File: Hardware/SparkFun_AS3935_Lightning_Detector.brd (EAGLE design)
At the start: 25.4 x 25.4 mm, 57 parts, among them U1 AS3935

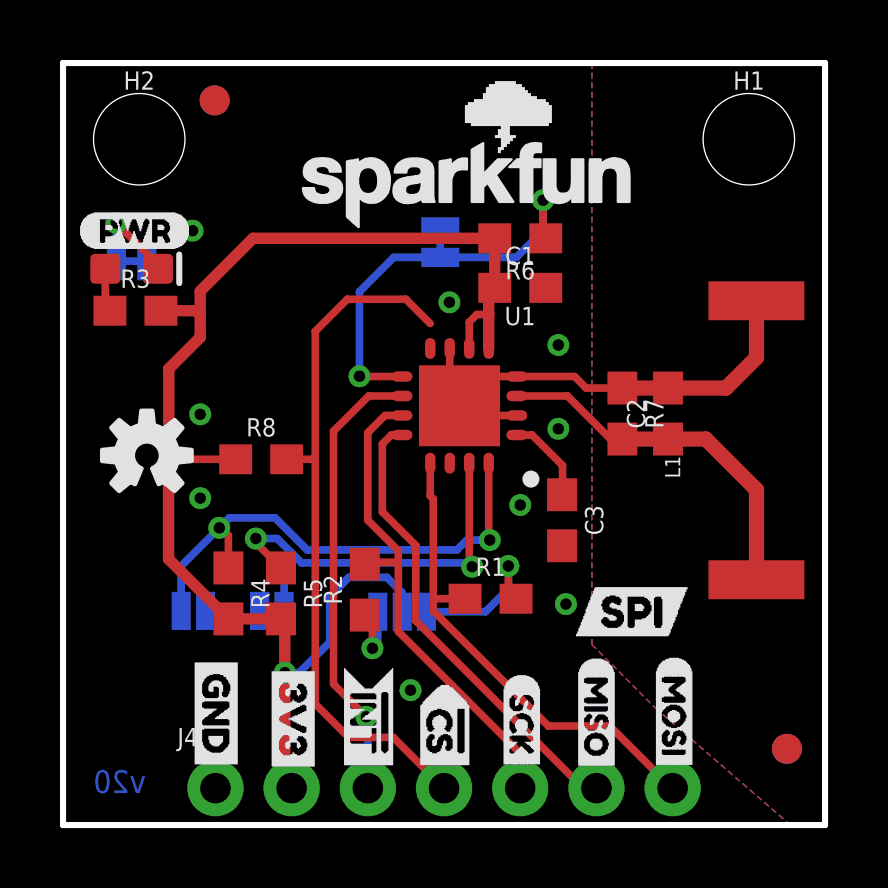
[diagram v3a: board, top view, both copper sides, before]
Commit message: Adds three way jumper for switching to I2C, one that also includes a way to ground Chip select
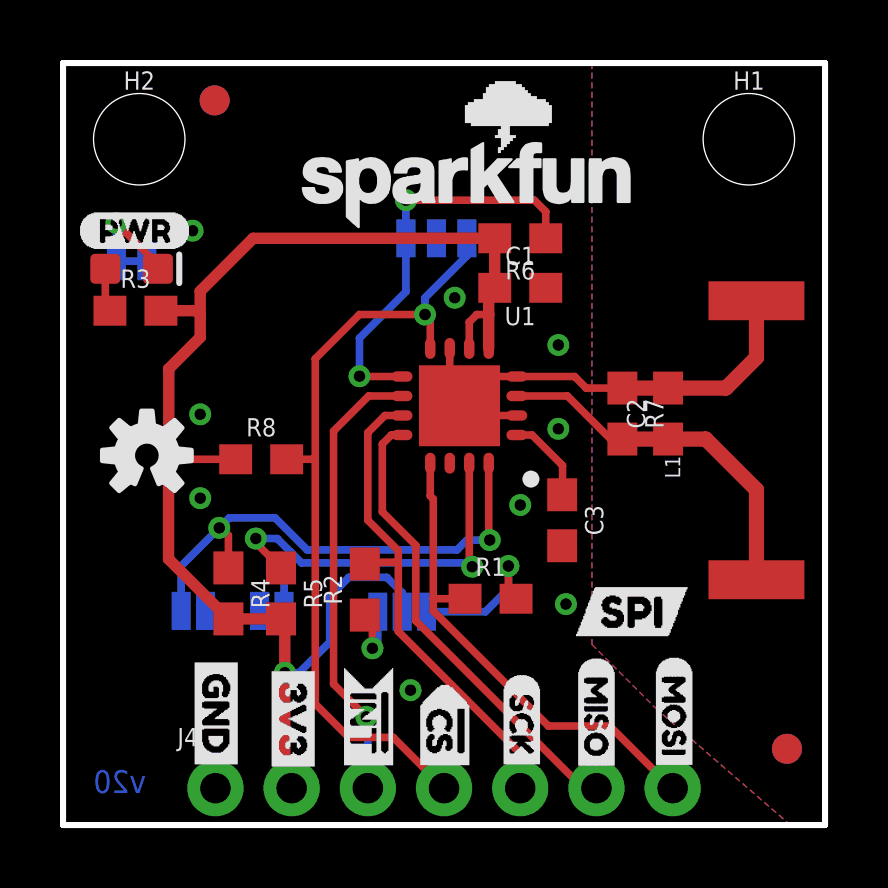
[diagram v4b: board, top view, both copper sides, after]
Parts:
- removed JP3: JUMPER-SMT_2_NC_TRACE_SILK, SparkFun-Jumpers:SMT-JUMPER_2_NC_TRACE_SILK
- added JP1: I2C_EN, SparkFun-Jumpers:SMT-JUMPER_3_1-NC_TRACE_SILK
- added U$16: (no value), CS and SI:CS0
- added U$19: (no value), CS and SI:SI1
- moved U$17 0.15 mm to (15.4, 21.7)
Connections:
- net !CS: now also JP1.1
- net GND: now also JP1.2; no longer JP3.2
- net SEL_INTER: now also JP1.3; no longer JP3.1
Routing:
- net !CS: track 23.4 -> 26.5 mm, vias 0 -> 1
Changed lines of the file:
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@@
 <attribute name="VALUE" value="10k" x="15.24" y="20.32" size="0.6096" layer="27" font="vector" ratio="20" rot="R180" align="top-center"/>
-</element>
-<element name="JP3" library="SparkFun-Jumpers" package="SMT-JUMPER_2_NC_TRACE_SILK" value="JUMPER-SMT_2_NC_TRACE_SILK" x="12.573" y="19.431" smashed="yes" rot="MR90">
-<attribute name="NAME" x="13.716" y="19.431" size="0.6096" layer="26" font="vector" ratio="20" rot="MR90" align="bottom-center"/>
-<attribute name="VALUE" x="11.43" y="19.431" size="0.6096" layer="28" font="vector" ratio="20" rot="MR90" align="top-center"/>
 </element>
 <element name="J4" library="SparkFun-Connectors" package="1X07_NO_SILK" value="" x="5.08" y="1.229359375" smashed="yes">
@@
 <element name="U$14" library="INT" package="#INT0" value="" x="10.1854" y="5.5118" smashed="yes" rot="MR270"/>
 <element name="U$15" library="DataLines" package="SPI1" value="" x="21.082" y="7.112" smashed="yes" rot="MR0"/>
-<element name="U$17" library="i2c_EN" package="I#C_EN0" value="" x="15.5194" y="21.6916" smashed="yes" rot="MR0"/>
+<element name="U$17" library="i2c_EN" package="I#C_EN0" value="" x="15.367" y="21.6916" smashed="yes" rot="MR0"/>
+<element name="JP1" library="SparkFun-Jumpers" package="SMT-JUMPER_3_1-NC_TRACE_SILK" value="I2C_EN" x="12.446" y="19.558" smashed="yes" rot="MR0">
+<attribute name="NAME" x="12.446" y="20.701" size="0.6096" layer="26" font="vector" ratio="20" rot="MR0" align="bottom-center"/>
+<attribute name="VALUE" x="12.446" y="18.415" size="0.6096" layer="28" font="vector" ratio="20" rot="MR0" align="top-center"/>
+</element>
+<element name="U$16" library="CS and SI" package="CS0" value="" x="15.0622" y="21.3868" smashed="yes" rot="MR270"/>
+<element name="U$19" library="CS and SI" package="SI1" value="" x="9.779" y="21.0312" smashed="yes" rot="MR270"/>
 </elements>
 <signals>
@@
 <contactref element="ADD0" pad="2"/>
 <contactref element="ADD1" pad="2"/>
-<contactref element="JP3" pad="2"/>
 <contactref element="J4" pad="1"/>
 <contactref element="C3" pad="2"/>
@@
 <via x="16.51" y="13.208" extent="1-16" drill="0.381"/>
 <via x="16.51" y="16.002" extent="1-16" drill="0.381"/>
-<via x="12.8778" y="17.4244" extent="1-16" drill="0.381"/>
+<via x="13.0556" y="17.5768" extent="1-16" drill="0.381"/>
 <via x="4.318" y="19.812" extent="1-16" drill="0.381"/>
 <wire x1="12.8896" y1="15.8866" x2="12.8896" y2="14.3016" width="0.254" layer="1"/>
@@
 <wire x1="23.114" y1="15.582" x2="23.114" y2="17.477" width="0.508" layer="1"/>
 <via x="4.572" y="10.8966" extent="1-16" drill="0.381"/>
+<contactref element="JP1" pad="2"/>
 </signal>
 <signal name="3.3V">
@@
 <signal name="SEL_INTER">
 <contactref element="R6" pad="1"/>
-<contactref element="JP3" pad="1"/>
 <contactref element="U1" pad="9"/>
-<via x="16.002" y="20.828" extent="1-16" drill="0.381"/>
-<wire x1="15.113" y1="18.923" x2="16.002" y2="19.812" width="0.254" layer="16"/>
-<wire x1="16.002" y1="19.812" x2="16.002" y2="20.828" width="0.254" layer="16"/>
-<wire x1="16.09" y1="19.558" x2="16.002" y2="19.646" width="0.254" layer="1"/>
-<wire x1="16.002" y1="19.646" x2="16.002" y2="20.828" width="0.254" layer="1"/>
 <wire x1="11.2996" y1="14.9516" x2="9.8896" y2="14.9516" width="0.254" layer="1"/>
 <wire x1="9.8806" y1="14.9606" x2="9.8896" y2="14.9516" width="0.254" layer="1"/>
 <via x="9.8806" y="14.9606" extent="1-16" drill="0.381"/>
-<wire x1="9.8806" y1="14.9606" x2="9.8806" y2="17.78" width="0.254" layer="16"/>
-<wire x1="9.8806" y1="17.78" x2="11.0236" y2="18.923" width="0.254" layer="16"/>
-<wire x1="11.0236" y1="18.923" x2="12.573" y2="18.923" width="0.254" layer="16"/>
-<wire x1="12.573" y1="18.923" x2="15.113" y2="18.923" width="0.254" layer="16"/>
+<contactref element="JP1" pad="3"/>
+<wire x1="11.43" y1="19.558" x2="11.43" y2="19.3294" width="0.2032" layer="16"/>
+<wire x1="11.43" y1="17.78" x2="11.43" y2="19.558" width="0.254" layer="16"/>
+<wire x1="9.8806" y1="14.9606" x2="9.8806" y2="16.2306" width="0.254" layer="16"/>
+<wire x1="9.8806" y1="16.2306" x2="11.43" y2="17.78" width="0.254" layer="16"/>
+<wire x1="11.43" y1="20.828" x2="11.43" y2="19.558" width="0.254" layer="16"/>
+<wire x1="16.09" y1="19.558" x2="16.002" y2="19.646" width="0.254" layer="1"/>
+<via x="11.43" y="20.828" extent="1-16" drill="0.381"/>
+<wire x1="16.09" y1="19.558" x2="16.09" y2="20.447" width="0.254" layer="1"/>
+<wire x1="16.09" y1="20.447" x2="15.709" y2="20.828" width="0.254" layer="1"/>
+<wire x1="15.709" y1="20.828" x2="11.43" y2="20.828" width="0.254" layer="1"/>
 </signal>
 <signal name="MISO">
@@
 <wire x1="11.008359375" y1="2.921" x2="9.525" y2="2.921" width="0.254" layer="1"/>
 <wire x1="9.525" y1="2.921" x2="8.4074" y2="4.0386" width="0.254" layer="1"/>
-<wire x1="12.2396" y1="16.7164" x2="11.43" y2="17.526" width="0.254" layer="1"/>
-<wire x1="9.4742" y1="17.526" x2="11.43" y2="17.526" width="0.254" layer="1"/>
-<wire x1="8.4074" y1="16.4592" x2="9.4742" y2="17.526" width="0.254" layer="1"/>
 <wire x1="8.4074" y1="4.0386" x2="8.4074" y2="12.192" width="0.254" layer="1"/>
-<wire x1="8.4074" y1="12.192" x2="8.4074" y2="16.4592" width="0.254" layer="1"/>
 <contactref element="U1" pad="8"/>
 <contactref element="R8" pad="2"/>
 <wire x1="7.454" y1="12.192" x2="8.4074" y2="12.192" width="0.254" layer="1"/>
-<wire x1="12.2396" y1="16.7164" x2="12.2396" y2="15.8866" width="0" layer="19" extent="1-1"/>
+<contactref element="JP1" pad="1"/>
+<wire x1="12.2396" y1="15.8866" x2="12.2428" y2="15.8898" width="0.2032" layer="1"/>
+<via x="12.065" y="17.018" extent="1-16" drill="0.381"/>
+<wire x1="13.462" y1="19.558" x2="13.462" y2="18.9738" width="0.254" layer="16"/>
+<wire x1="13.462" y1="18.9738" x2="12.065" y2="17.5768" width="0.254" layer="16"/>
+<wire x1="12.065" y1="17.5768" x2="12.065" y2="17.018" width="0.254" layer="16"/>
+<wire x1="12.065" y1="17.018" x2="9.8806" y2="17.018" width="0.254" layer="1"/>
+<wire x1="12.2396" y1="15.8866" x2="12.2396" y2="16.8434" width="0.254" layer="1"/>
+<wire x1="12.2396" y1="16.8434" x2="12.065" y2="17.018" width="0.254" layer="1"/>
+<wire x1="8.4074" y1="12.192" x2="8.4074" y2="15.5448" width="0.254" layer="1"/>
+<wire x1="8.4074" y1="15.5448" x2="9.8806" y2="17.018" width="0.254" layer="1"/>
 </signal>
 <signal name="N$2">

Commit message: Adds measurements for the standoff holes, rotates CS and SI silk, removes some wire stubs.
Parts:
- moved U$16 2.86 mm to (17.2, 19.5), turned to 0 degrees
- moved U$19 2.09 mm to (11.2, 19.5), turned to 0 degrees
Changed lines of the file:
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@@
 <layer number="45" name="Holes" color="7" fill="1" visible="yes" active="yes"/>
 <layer number="46" name="Milling" color="3" fill="1" visible="no" active="yes"/>
-<layer number="47" name="Measures" color="7" fill="1" visible="no" active="yes"/>
+<layer number="47" name="Measures" color="7" fill="1" visible="yes" active="yes"/>
 <layer number="48" name="Document" color="7" fill="1" visible="no" active="yes"/>
 <layer number="49" name="Reference" color="13" fill="1" visible="yes" active="yes"/>
@@
 <wire x1="0" y1="0" x2="25.4" y2="0" width="0.2032" layer="20"/>
 <wire x1="25.4" y1="0" x2="25.4" y2="25.4" width="0.2032" layer="20"/>
-<wire x1="25.4" y1="25.4" x2="0" y2="25.4" width="0.2032" layer="20"/>
 <wire x1="0" y1="25.4" x2="0" y2="0" width="0.2032" layer="20"/>
 <text x="19.177" y="-19.177" size="1.778" layer="51" font="vector">Elias Santistevan</text>
 <text x="2.7686" y="1.0668" size="0.762" layer="16" font="vector" ratio="15" rot="MR0">v20</text>
-<dimension x1="25.4" y1="25.4" x2="0" y2="25.4" x3="12.7" y3="28.194" textsize="1.778" textratio="15" layer="47" dtype="horizontal" unit="inch"/>
 <dimension x1="25.4" y1="0" x2="25.4" y2="25.4" x3="30.226" y3="12.7" textsize="1.778" textratio="15" layer="47" dtype="horizontal" unit="inch"/>
 <text x="4.318" y="-4.572" size="1.778" layer="47" font="vector" ratio="15">Units in Inches</text>
+<dimension x1="25.4" y1="25.4" x2="0" y2="25.4" x3="12.7" y3="30.988" textsize="1.778" textratio="15" layer="47" dtype="horizontal" unit="inch"/>
+<dimension x1="2.54" y1="22.86" x2="0" y2="22.86" x3="1.27" y3="27.178" textsize="1.778" textratio="15" layer="47" dtype="horizontal" unit="inch"/>
+<wire x1="25.4" y1="25.4" x2="0" y2="25.4" width="0.2032" layer="20"/>
+<dimension x1="22.86" y1="22.86" x2="22.86" y2="25.4" x3="28.448" y3="24.13" textsize="1.778" textratio="15" layer="20" dtype="horizontal" unit="inch"/>
 </plain>
 <attributes>
@@
 <attribute name="VALUE" x="12.446" y="18.415" size="0.6096" layer="28" font="vector" ratio="20" rot="MR0" align="top-center"/>
 </element>
-<element name="U$16" library="CS and SI" package="CS0" value="" x="15.0622" y="21.3868" smashed="yes" rot="MR270"/>
-<element name="U$19" library="CS and SI" package="SI1" value="" x="9.779" y="21.0312" smashed="yes" rot="MR270"/>
+<element name="U$16" library="CS and SI" package="CS0" value="" x="17.2212" y="19.5072" smashed="yes" rot="MR0"/>
+<element name="U$19" library="CS and SI" package="SI1" value="" x="11.176" y="19.4818" smashed="yes" rot="MR0"/>
 </elements>
 <signals>
@@
 <via x="9.8806" y="14.9606" extent="1-16" drill="0.381"/>
 <contactref element="JP1" pad="3"/>
-<wire x1="11.43" y1="19.558" x2="11.43" y2="19.3294" width="0.2032" layer="16"/>
 <wire x1="11.43" y1="17.78" x2="11.43" y2="19.558" width="0.254" layer="16"/>
 <wire x1="9.8806" y1="14.9606" x2="9.8806" y2="16.2306" width="0.254" layer="16"/>
 <wire x1="9.8806" y1="16.2306" x2="11.43" y2="17.78" width="0.254" layer="16"/>
 <wire x1="11.43" y1="20.828" x2="11.43" y2="19.558" width="0.254" layer="16"/>
-<wire x1="16.09" y1="19.558" x2="16.002" y2="19.646" width="0.254" layer="1"/>
 <via x="11.43" y="20.828" extent="1-16" drill="0.381"/>
 <wire x1="16.09" y1="19.558" x2="16.09" y2="20.447" width="0.254" layer="1"/>
@@
 <wire x1="7.454" y1="12.192" x2="8.4074" y2="12.192" width="0.254" layer="1"/>
 <contactref element="JP1" pad="1"/>
-<wire x1="12.2396" y1="15.8866" x2="12.2428" y2="15.8898" width="0.2032" layer="1"/>
 <via x="12.065" y="17.018" extent="1-16" drill="0.381"/>
 <wire x1="13.462" y1="19.558" x2="13.462" y2="18.9738" width="0.254" layer="16"/>
